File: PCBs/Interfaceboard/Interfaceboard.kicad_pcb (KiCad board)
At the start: 2 copper layers, 80 x 80 mm, 64 parts, among them J301 TSW-105-07-T-D, J302 TSW-105-07-T-D, J304 TSW-105-07-T-D, J305 TSW-105-07-T-D, SW1 PTS645, U1 AD8420ARMZ, U2 AD8420ARMZ, U3 MCP6L01x-xOT

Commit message: Changed M2 to M3 hole. Vias are free.
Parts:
- H1, H2: value M2 Mount -> M3 Mount; footprint MountingHole:MountingHole_2.1mm -> MountingHole:MountingHole_3.2mm_M3
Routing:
- net GND: vias 124 -> 153

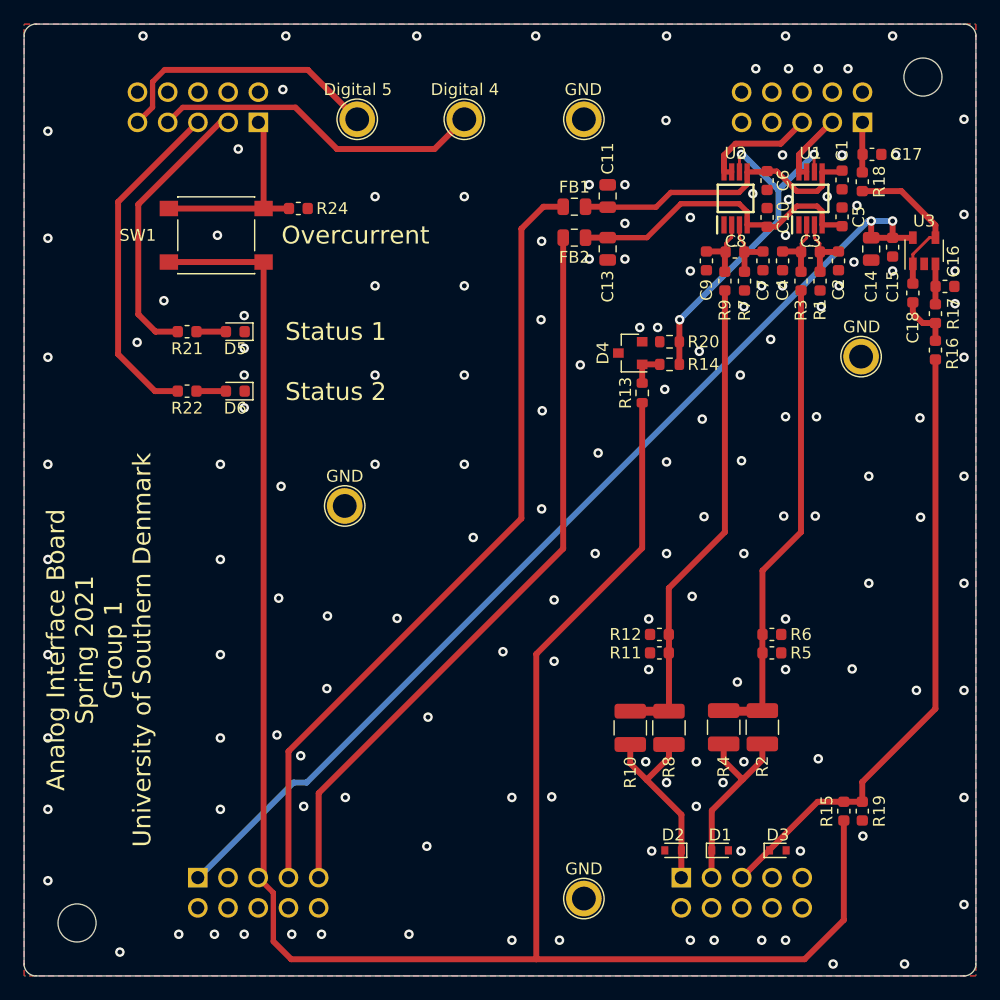
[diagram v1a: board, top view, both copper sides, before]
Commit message: Swapped some ADC channels for the signals to ensure that simultaneous conversion is possible.
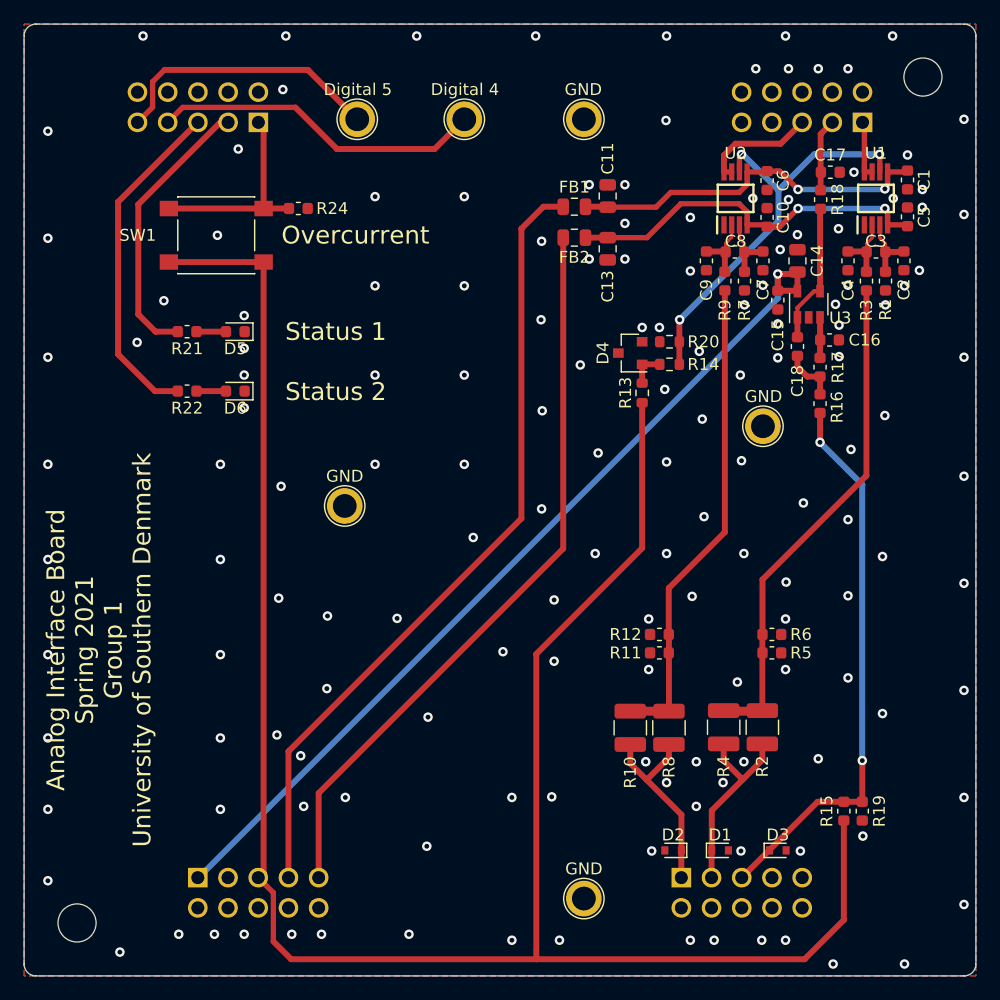
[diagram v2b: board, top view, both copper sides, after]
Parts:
- moved C16 10.7 mm to (172.7, 76.5)
- moved U3 10.7 mm to (170.9, 73.5)
- moved C18 10.7 mm to (170.0, 77.1)
- moved R16 10.7 mm to (171.9, 81.9)
- moved R17 10.7 mm to (171.9, 78.8)
- moved C15 10.6 mm to (168.3, 73.2)
- moved TP5 10.1 mm to (167.1, 83.8)
- moved C14 6.28 mm to (170.0, 69.9), turned to 90 degrees
- moved C1 5.50 mm to (179.2, 63.1)
- moved C2 5.50 mm to (178.9, 69.9)
- moved C3 5.50 mm to (176.6, 69.2)
- moved C4 5.50 mm to (174.2, 69.9)
- moved C5 5.50 mm to (179.2, 66.2)
- moved R1 5.50 mm to (177.4, 71.6)
- moved R3 5.50 mm to (175.8, 71.6)
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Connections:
- C17 pad 1: /Connectors/ADC1 -> /Connectors/ADC3
- R18 pad 1: /Connectors/ADC1 -> /Connectors/ADC3
- U1 pad 7: /Connectors/ADC3 -> /Connectors/ADC1
- U1 pad 8: /Connectors/ADC3 -> /Connectors/ADC1
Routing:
- net +5V: track 87.6 -> 77.2 mm, vias 2 -> 1
- net /Connectors/Torque_Meas: track 52.5 -> 46.9 mm, vias 0 -> 2
- net /Currents/0V5: track 29.7 -> 35.3 mm
- net /Currents/+15V_Filt: track 25.6 -> 30.9 mm, vias 0 -> 2
- net /Currents/-15V_Filt: track 26.3 -> 31.6 mm, vias 0 -> 2
- net Net-(R2-Pad1): track 39.9 -> 42.2 mm
- net Net-(C18-Pad1): track 13.5 -> 12.1 mm
- net /Connectors/ADC1: track 4.21 -> 4.91 mm
- net GND: vias 153 -> 155

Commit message: Made minor changes to PCB to accommodate review feedback.
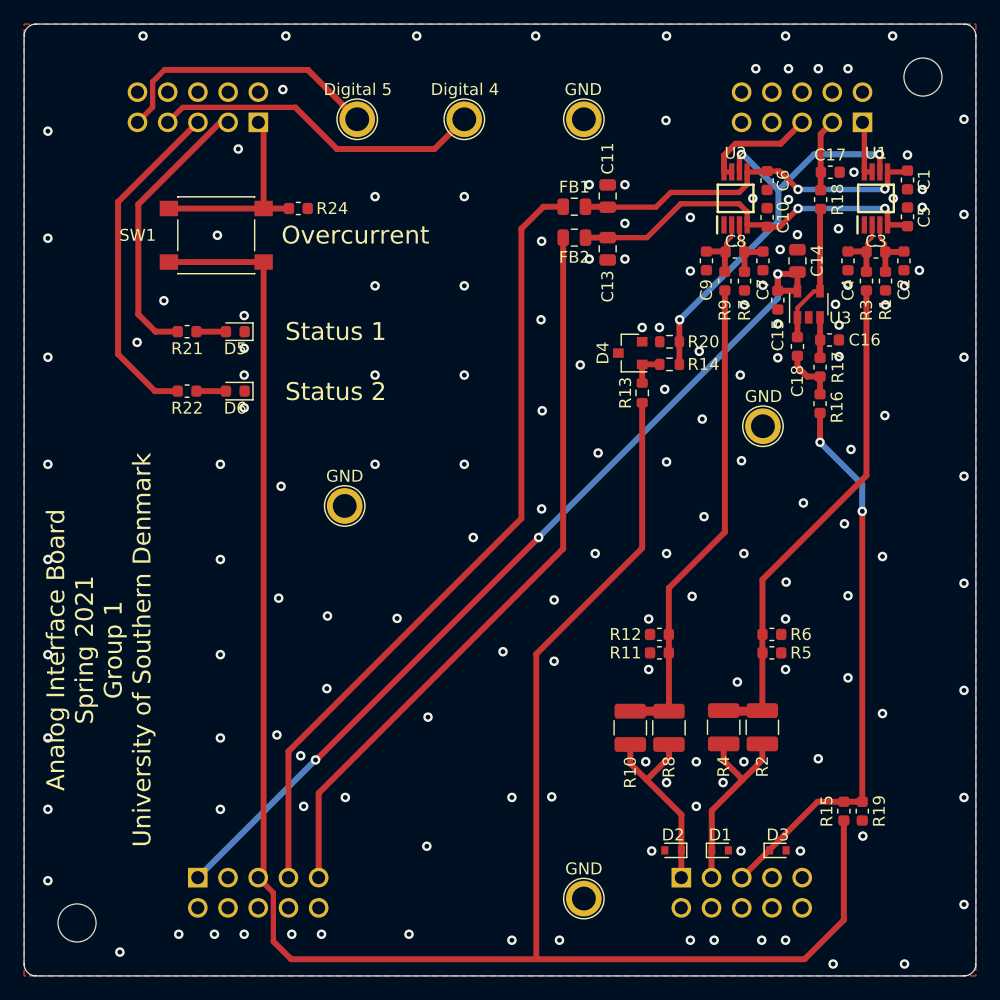
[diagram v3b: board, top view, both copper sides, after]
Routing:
- net +5V: vias 1 -> 3
